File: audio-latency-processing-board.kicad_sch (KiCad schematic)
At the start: 0 parts

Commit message: [#71107] Design initial schematic
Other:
- added sheet ADC (adc.kicad_sch)
- added sheet IO (IO.kicad_sch)
- added sheet Left Ear Microphone Connector (L_ear_conn.kicad_sch)
- added sheet Right Ear Microphone Connector (R_ear_conn.kicad_sch)
- added sheet Speaker + AMP (amp.kicad_sch)
- added sheet USB + Power (usb.kicad_sch)

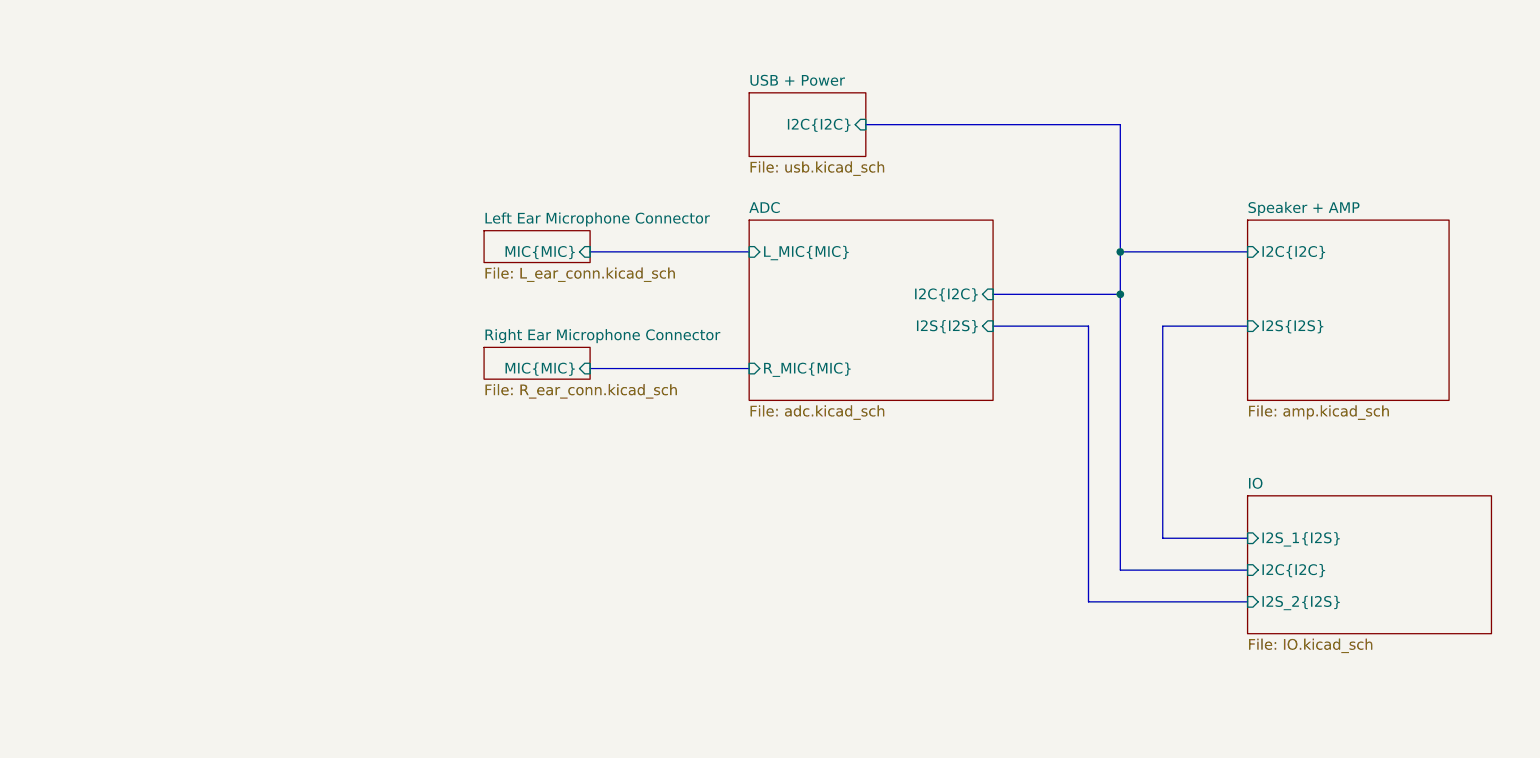
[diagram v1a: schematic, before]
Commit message: [#71555] Add new root sheet structure
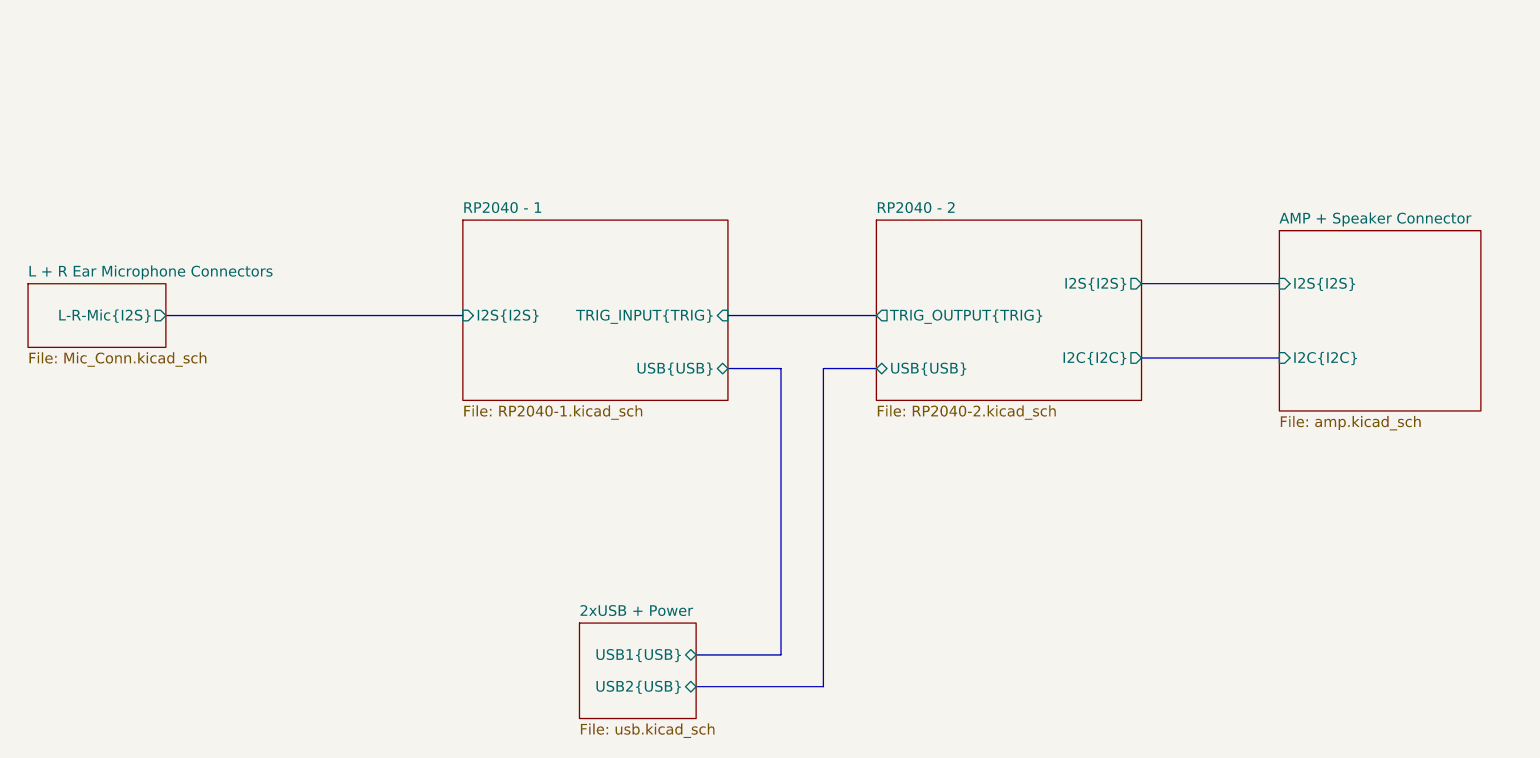
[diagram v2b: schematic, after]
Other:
- sheet Speaker + AMP renamed AMP + Speaker Connector
- sheet USB + Power renamed 2xUSB + Power
- removed sheet ADC
- removed sheet IO
- removed sheet Left Ear Microphone Connector
- removed sheet Right Ear Microphone Connector
- added sheet L + R Ear Microphone Connectors (Mic_Conn.kicad_sch)
- added sheet RP2040 - 1 (RP2040-1.kicad_sch)
- added sheet RP2040 - 2 (RP2040-2.kicad_sch)
- sheet 2xUSB + Power ports: added USB1{USB}, USB2{USB}; removed I2C{I2C}

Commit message: [#71555] Add connections between RP2040s
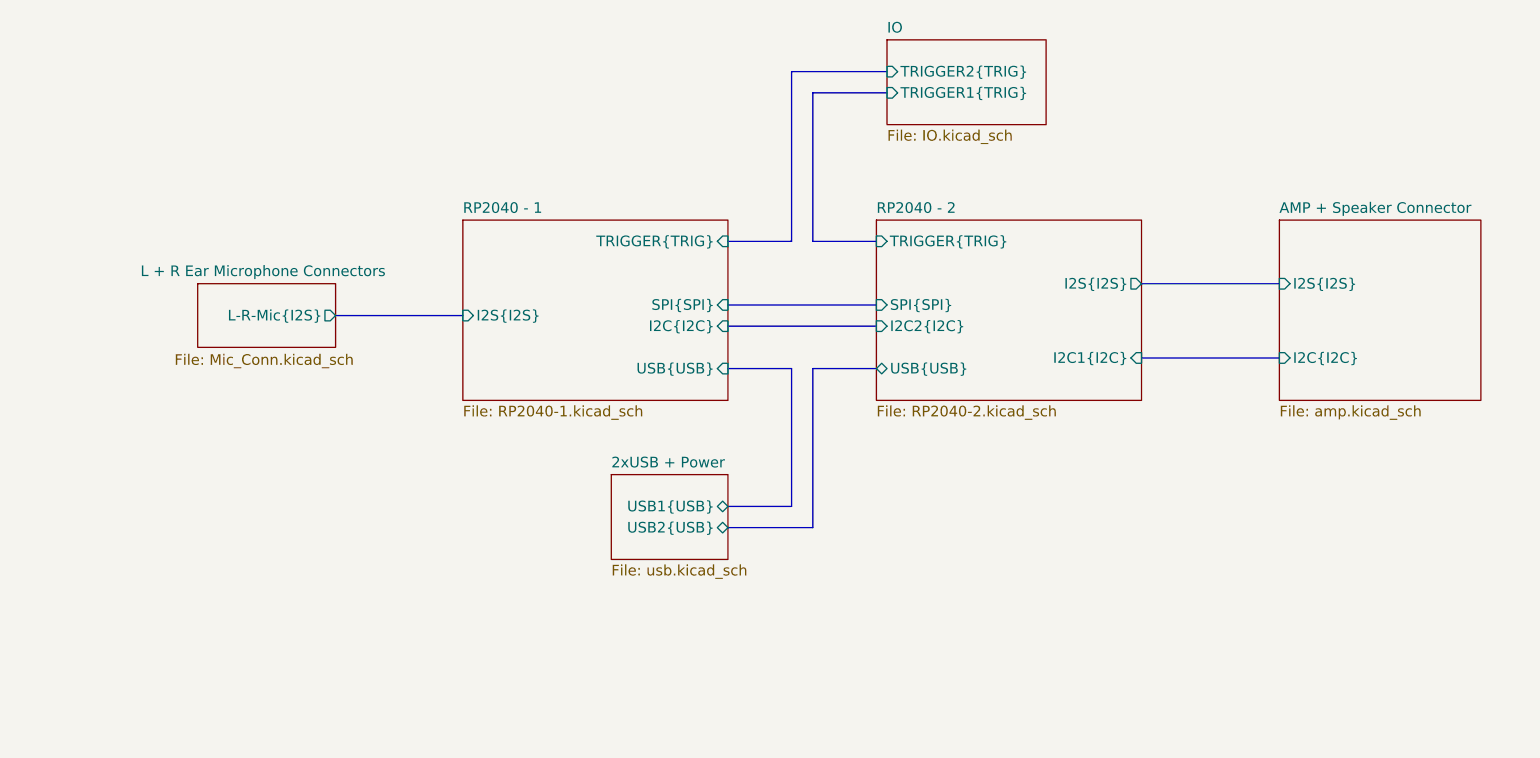
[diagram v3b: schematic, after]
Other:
- added sheet IO (IO.kicad_sch)
- sheet RP2040 - 1 ports: added I2C{I2C}, SPI{SPI}, TRIGGER{TRIG}; removed TRIG_INPUT{TRIG}
- sheet RP2040 - 2 ports: added I2C1{I2C}, I2C2{I2C}, SPI{SPI}, TRIGGER{TRIG}; removed I2C{I2C}, TRIG_OUTPUT{TRIG}
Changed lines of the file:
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@@
 		(members "SD" "SCK" "WS")
 	)
+	(bus_alias "SPI"
+		(members "MISO" "MOSI" "SCK" "~{CS1}" "~{CS2}")
+	)
 	(bus_alias "TRIG"
-		(members "TRIG")
-	)
-	(bus
-		(pts
-			(xy 194.31 176.53) (xy 194.31 138.43)
-		)
-		(stroke
-			(width 0)
-			(type default)
-		)
-	)
-	(bus
-		(pts
-			(xy 115.57 132.08) (xy 151.13 132.08)
+		(members "TRIG1" "TRIG2" "TRIG3")
+	)
+	(bus
+		(pts
+			(xy 193.04 157.48) (xy 193.04 138.43)
+		)
+		(stroke
+			(width 0)
+			(type default)
+		)
+	)
+	(bus
+		(pts
+			(xy 135.89 132.08) (xy 151.13 132.08)
 		)
 		(stroke
@@
 	(bus
 		(pts
-			(xy 189.23 172.72) (xy 189.23 138.43)
-		)
-		(stroke
-			(width 0)
-			(type default)
-		)
-	)
-	(bus
-		(pts
-			(xy 179.07 172.72) (xy 189.23 172.72)
-		)
-		(stroke
-			(width 0)
-			(type default)
-		)
-	)
-	(bus
-		(pts
-			(xy 182.88 132.08) (xy 200.66 132.08)
-		)
-		(stroke
-			(width 0)
-			(type default)
-			(color 0 175 145 1)
+			(xy 190.5 154.94) (xy 190.5 138.43)
+		)
+		(stroke
+			(width 0)
+			(type default)
+		)
+	)
+	(bus
+		(pts
+			(xy 182.88 157.48) (xy 193.04 157.48)
+		)
+		(stroke
+			(width 0)
+			(type default)
+		)
+	)
+	(bus
+		(pts
+			(xy 182.88 154.94) (xy 190.5 154.94)
+		)
+		(stroke
+			(width 0)
+			(type default)
+		)
+	)
+	(bus
+		(pts
+			(xy 182.88 123.19) (xy 190.5 123.19)
+		)
+		(stroke
+			(width 0)
+			(type default)
+		)
+	)
+	(bus
+		(pts
+			(xy 193.04 105.41) (xy 201.93 105.41)
+		)
+		(stroke
+			(width 0)
+			(type default)
+		)
+	)
+	(bus
+		(pts
+			(xy 182.88 130.81) (xy 200.66 130.81)
+		)
+		(stroke
+			(width 0)
+			(type default)
+		)
+	)
+	(bus
+		(pts
+			(xy 182.88 133.35) (xy 200.66 133.35)
+		)
+		(stroke
+			(width 0)
+			(type default)
+		)
+	)
+	(bus
+		(pts
+			(xy 193.04 123.19) (xy 200.66 123.19)
+		)
+		(stroke
+			(width 0)
+			(type default)
 		)
 	)
@@
 	(bus
 		(pts
-			(xy 189.23 138.43) (xy 182.88 138.43)
-		)
-		(stroke
-			(width 0)
-			(type default)
-		)
-	)
-	(bus
-		(pts
-			(xy 179.07 176.53) (xy 194.31 176.53)
-		)
-		(stroke
-			(width 0)
-			(type default)
-		)
-	)
-	(bus
-		(pts
-			(xy 194.31 138.43) (xy 200.66 138.43)
+			(xy 193.04 105.41) (xy 193.04 123.19)
+		)
+		(stroke
+			(width 0)
+			(type default)
+		)
+	)
+	(bus
+		(pts
+			(xy 190.5 138.43) (xy 182.88 138.43)
+		)
+		(stroke
+			(width 0)
+			(type default)
+		)
+	)
+	(bus
+		(pts
+			(xy 193.04 138.43) (xy 200.66 138.43)
+		)
+		(stroke
+			(width 0)
+			(type default)
+		)
+	)
+	(bus
+		(pts
+			(xy 190.5 102.87) (xy 201.93 102.87)
+		)
+		(stroke
+			(width 0)
+			(type default)
+		)
+	)
+	(bus
+		(pts
+			(xy 190.5 123.19) (xy 190.5 102.87)
 		)
 		(stroke
@@
 			)
 		)
-		(pin "TRIG_INPUT{TRIG}" input
-			(at 182.88 132.08 0)
-			(effects
-				(font
-					(size 1.27 1.27)
-				)
-				(justify right)
-			)
-		)
-		(pin "USB{USB}" bidirectional
+		(pin "USB{USB}" input
 			(at 182.88 138.43 0)
+			(effects
+				(font
+					(size 1.27 1.27)
+				)
+				(justify right)
+			)
+		)
+		(pin "I2C{I2C}" input
+			(at 182.88 133.35 0)
+			(effects
+				(font
+					(size 1.27 1.27)
+				)
+				(justify right)
+			)
+		)
+		(pin "TRIGGER{TRIG}" input
+			(at 182.88 123.19 0)
+			(effects
+				(font
+					(size 1.27 1.27)
+				)
+				(justify right)
+			)
+		)
+		(pin "SPI{SPI}" input
+			(at 182.88 130.81 0)
 			(effects
 				(font
@@
 	)
 	(sheet
-		(at 165.1 168.91)
-		(size 13.97 11.43)
+		(at 201.93 99.06)
+		(size 19.05 10.16)
 		(fields_autoplaced yes)
 		(stroke
@@
 			(color 0 0 0 0.0000)
 		)
+		(property "Sheetname" "IO"
+			(at 201.93 98.3484 0)
+			(effects
+				(font
+					(size 1.27 1.27)
+				)
+				(justify left bottom)
+			)
+		)
+		(property "Sheetfile" "IO.kicad_sch"
+			(at 201.93 109.8046 0)
+			(effects
+				(font
+					(size 1.27 1.27)
+				)
+				(justify left top)
+			)
+		)
+		(pin "TRIGGER1{TRIG}" input
+			(at 201.93 105.41 180)
+			(effects
+				(font
+					(size 1.27 1.27)
+				)
+				(justify left)
+			)
+		)
+		(pin "TRIGGER2{TRIG}" input
+			(at 201.93 102.87 180)
+			(effects
+				(font
+					(size 1.27 1.27)
+				)
+				(justify left)
+			)
+		)
+		(instances
+			(project "audio-latency-processing-board"
+				(path "/7fb12ebf-f685-4412-b638-445b1bf344bc"
+					(page "7")
+				)
+			)
+		)
+	)
+	(sheet
+		(at 168.91 151.13)
+		(size 13.97 10.16)
+		(fields_autoplaced yes)
+		(stroke
+			(width 0.1524)
+			(type solid)
+		)
+		(fill
+			(color 0 0 0 0.0000)
+		)
 		(property "Sheetname" "2xUSB + Power"
-			(at 165.1 168.1984 0)
+			(at 168.91 150.4184 0)
 			(effects
 				(font
@@
 		)
 		(property "Sheetfile" "usb.kicad_sch"
-			(at 165.1 180.9246 0)
+			(at 168.91 161.8746 0)
 			(effects
 				(font
@@
 		)
 		(pin "USB2{USB}" bidirectional
-			(at 179.07 176.53 0)
+			(at 182.88 157.48 0)
 			(effects
 				(font
@@
 		)
 		(pin "USB1{USB}" bidirectional
-			(at 179.07 172.72 0)
+			(at 182.88 154.94 0)
 			(effects
 				(font
@@
 	)
 	(sheet
-		(at 248.92 121.92)
+		(at 248.92 120.65)
 		(size 24.13 21.59)
 		(fields_autoplaced yes)
@@
 		)
 		(property "Sheetname" "AMP + Speaker Connector"
-			(at 248.92 121.2084 0)
+			(at 248.92 119.9384 0)
 			(effects
 				(font
@@
 		)
 		(property "Sheetfile" "amp.kicad_sch"
-			(at 248.92 144.0946 0)
+			(at 248.92 142.8246 0)
 			(effects
 				(font
@@
 	)
 	(sheet
-		(at 99.06 128.27)
+		(at 119.38 128.27)
 		(size 16.51 7.62)
-		(fields_autoplaced yes)
 		(stroke
 			(width 0.1524)
@@
 		)
 		(property "Sheetname" "L + R Ear Microphone Connectors"
-			(at 99.06 127.5584 0)
+			(at 112.522 127.508 0)
 			(effects
 				(font
@@
 		)
 		(property "Sheetfile" "Mic_Conn.kicad_sch"
-			(at 99.06 136.4746 0)
+			(at 116.586 136.652 0)
 			(effects
 				(font
@@
 		)
 		(pin "L-R-Mic{I2S}" output
-			(at 115.57 132.08 0)
+			(at 135.89 132.08 0)
 			(effects
 				(font
@@
 			)
 		)
-		(pin "I2C{I2C}" output
-			(at 232.41 137.16 0)
-			(effects
-				(font
-					(size 1.27 1.27)
-				)
-				(justify right)
-			)
-		)
-		(pin "TRIG_OUTPUT{TRIG}" output
-			(at 200.66 132.08 180)
-			(effects
-				(font
-					(size 1.27 1.27)
-				)
-				(justify left)
-			)
-		)
 		(pin "USB{USB}" bidirectional
 			(at 200.66 138.43 180)
 			(effects
 				(font
+					(size 1.27 1.27)
+				)
+				(justify left)
+			)
+		)
+		(pin "TRIGGER{TRIG}" input
+			(at 200.66 123.19 180)
+			(effects
+				(font
+					(size 1.27 1.27)
+				)
+				(justify left)
+			)
+		)
+		(pin "SPI{SPI}" input
+			(at 200.66 130.81 180)
+			(effects
+				(font
+					(size 1.27 1.27)
+				)
+				(justify left)
+			)
+		)
+		(pin "I2C1{I2C}" input
+			(at 232.41 137.16 0)
+			(effects
+				(font
+					(size 1.27 1.27)
+				)
+				(justify right)
+			)
+		)
+		(pin "I2C2{I2C}" input
+			(at 200.66 133.35 180)
+			(effects
+				(font

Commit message: [#71555] Resolve ERC
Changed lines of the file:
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@@
 	(bus
 		(pts
-			(xy 193.04 157.48) (xy 193.04 138.43)
+			(xy 194.31 157.48) (xy 194.31 138.43)
 		)
 		(stroke
@@
 	(bus
 		(pts
-			(xy 182.88 157.48) (xy 193.04 157.48)
+			(xy 182.88 157.48) (xy 194.31 157.48)
+		)
+		(stroke
+			(width 0)
+			(type default)
+		)
+	)
+	(bus
+		(pts
+			(xy 194.31 106.68) (xy 201.93 106.68)
 		)
 		(stroke
@@
 	(bus
 		(pts
-			(xy 193.04 105.41) (xy 201.93 105.41)
-		)
-		(stroke
-			(width 0)
-			(type default)
-		)
-	)
-	(bus
-		(pts
-			(xy 182.88 130.81) (xy 200.66 130.81)
-		)
-		(stroke
-			(width 0)
-			(type default)
+			(xy 194.31 123.19) (xy 200.66 123.19)
+		)
+		(stroke
+			(width 0)
+			(type default)
+		)
+	)
+	(bus
+		(pts
+			(xy 232.41 128.27) (xy 248.92 128.27)
+		)
+		(stroke
+			(width 0)
+			(type default)
+			(color 241 95 50 1)
 		)
 	)
@@
 	(bus
 		(pts
-			(xy 193.04 123.19) (xy 200.66 123.19)
-		)
-		(stroke
-			(width 0)
-			(type default)
-		)
-	)
-	(bus
-		(pts
-			(xy 232.41 128.27) (xy 248.92 128.27)
-		)
-		(stroke
-			(width 0)
-			(type default)
-			(color 241 95 50 1)
-		)
-	)
-	(bus
-		(pts
 			(xy 232.41 137.16) (xy 248.92 137.16)
 		)
@@
 	(bus
 		(pts
-			(xy 193.04 105.41) (xy 193.04 123.19)
+			(xy 194.31 106.68) (xy 194.31 123.19)
 		)
 		(stroke
@@
 	(bus
 		(pts
-			(xy 193.04 138.43) (xy 200.66 138.43)
+			(xy 182.88 129.54) (xy 200.66 129.54)
+		)
+		(stroke
+			(width 0)
+			(type default)
+		)
+	)
+	(bus
+		(pts
+			(xy 194.31 138.43) (xy 200.66 138.43)
 		)
 		(stroke
@@
 			)
 		)
+		(pin "I2C{I2C}" input
+			(at 182.88 133.35 0)
+			(effects
+				(font
+					(size 1.27 1.27)
+				)
+				(justify right)
+			)
+		)
+		(pin "TRIGGER{TRIG}" input
+			(at 182.88 123.19 0)
+			(effects
+				(font
+					(size 1.27 1.27)
+				)
+				(justify right)
+			)
+		)
+		(pin "SPI{SPI}" input
+			(at 182.88 129.54 0)
+			(effects
+				(font
+					(size 1.27 1.27)
+				)
+				(justify right)
+			)
+		)
 		(pin "USB{USB}" input
 			(at 182.88 138.43 0)
-			(effects
-				(font
-					(size 1.27 1.27)
-				)
-				(justify right)
-			)
-		)
-		(pin "I2C{I2C}" input
-			(at 182.88 133.35 0)
-			(effects
-				(font
-					(size 1.27 1.27)
-				)
-				(justify right)
-			)
-		)
-		(pin "TRIGGER{TRIG}" input
-			(at 182.88 123.19 0)
-			(effects
-				(font
-					(size 1.27 1.27)
-				)
-				(justify right)
-			)
-		)
-		(pin "SPI{SPI}" input
-			(at 182.88 130.81 0)
 			(effects
 				(font
@@
 	)
 	(sheet
-		(at 201.93 99.06)
-		(size 19.05 10.16)
+		(at 201.93 100.33)
+		(size 19.05 8.89)
 		(fields_autoplaced yes)
 		(stroke
@@
 		)
 		(property "Sheetname" "IO"
-			(at 201.93 98.3484 0)
+			(at 201.93 99.6184 0)
 			(effects
 				(font
@@
 		)
 		(pin "TRIGGER1{TRIG}" input
-			(at 201.93 105.41 180)
+			(at 201.93 106.68 180)
 			(effects
 				(font
@@
 			)
 		)
-		(pin "USB{USB}" bidirectional
-			(at 200.66 138.43 180)
-			(effects
-				(font
-					(size 1.27 1.27)
-				)
-				(justify left)
-			)
-		)
 		(pin "TRIGGER{TRIG}" input
 			(at 200.66 123.19 180)
@@
 		)
 		(pin "SPI{SPI}" input
-			(at 200.66 130.81 180)
+			(at 200.66 129.54 180)
 			(effects
 				(font
@@
 			(effects
 				(font
+					(size 1.27 1.27)
+				)
+				(justify left)
+			)
+		)
+		(pin "USB{USB}" input
+			(at 200.66 138.43 180)
+			(effects
+				(font
